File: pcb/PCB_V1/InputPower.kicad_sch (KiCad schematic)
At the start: 15 parts, among them J901 12 V IN / 25 A design, Q901 NTMFS5C628NLT1G, U901 LM74700QDBVRQ1

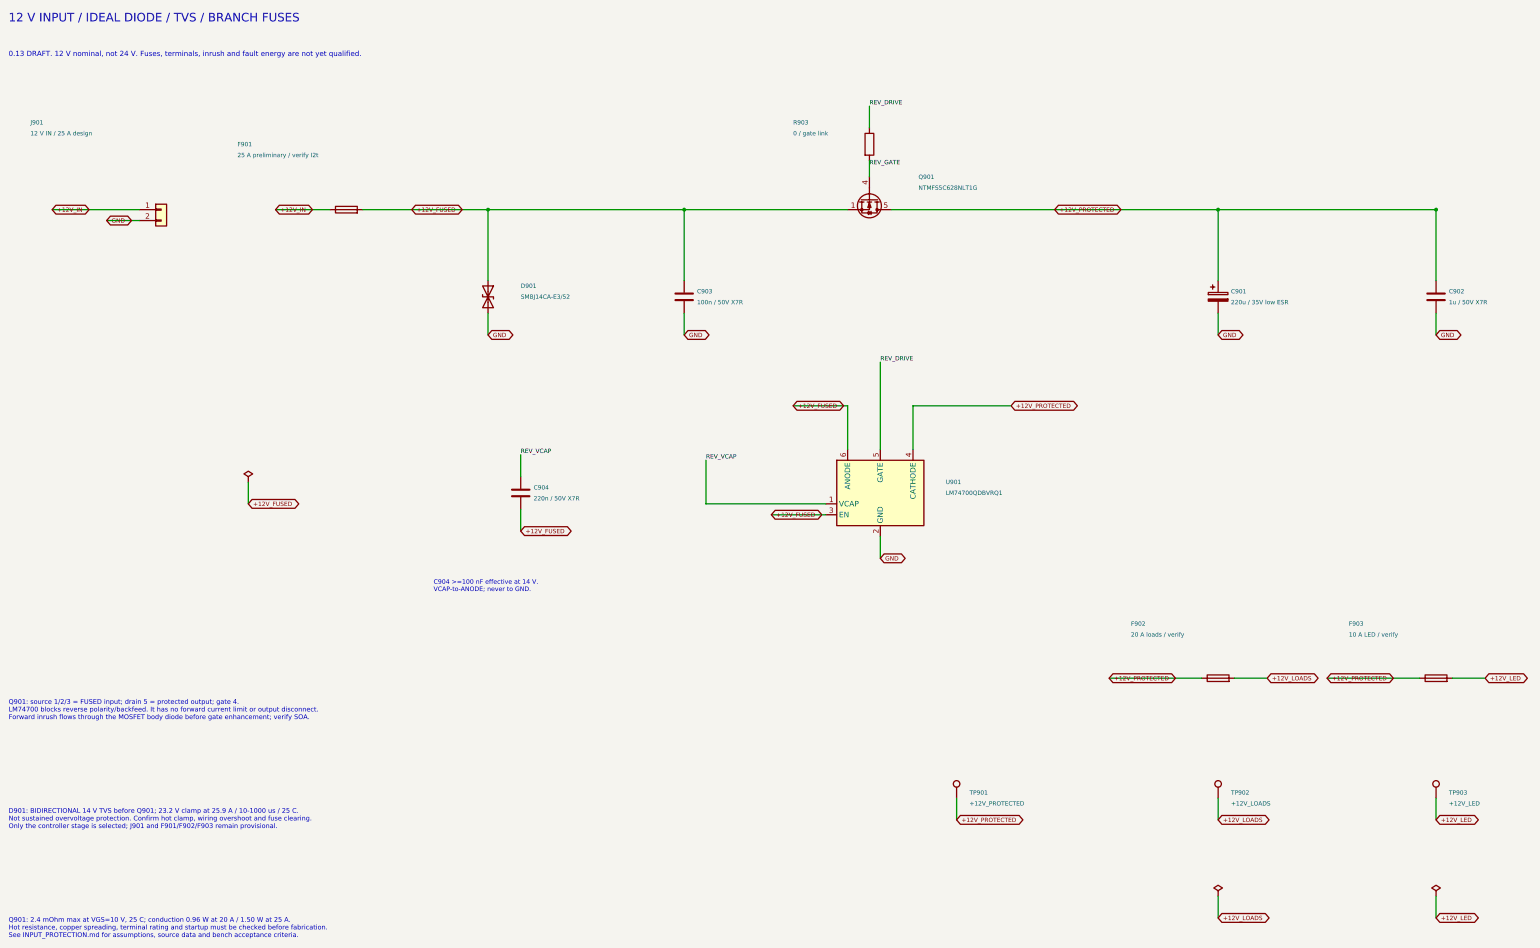
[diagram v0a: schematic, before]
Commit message: pcb: move board to 24 V input with 12 V aux buck and merged LED bar channel
Revision 0.14 of PCB_V1 (see pcb/PCB_V1/REDESIGN_24V.md):
- 24 V input on keyed XT60PW-M (pin 1 GND, pin 2 +24V); LM74700, input
  MOSFET and F901 removed; SMBJ26CA TVS; 220 uF/50 V bulk
- ATM mini-blade fuses in XF-508P-B-B holders: F902 10 A loads, F903 7.5 A LED
- new LMR16020 24 V -> 12 V aux buck (500 kHz) feeding PC fans, the
  UCC27524A heater gate driver and the TPS54202 3.3 V buck; TPS70950 removed
- heater and pump on 24 V: SMBJ30A drain TVS, AO3422 + SS36 pump stage
- LED CH1 panel keeps SRP1770TA/0.027 R/1k, switch now CSD19534Q5A;
  CH2 drives both identical bars in parallel (J721 || J731, 0.40 R);
  third AL8853 channel removed
- TS-1187A buttons, DORABO/KANGNEX terminals
- project library: LMR16020 and CSD19534Q5A symbols, TI DQJ and XF-508P
  footprints
- verify_netlist.py / verify_board.py / analyze_*.py updated for 24 V;
  new sync_board.py updates the unrouted staging board from the netlist
- ERC 0/0; netlist, board and sizing checks pass; DRC only the 12 known
  ESP32 drill sizes plus unrouted connections; 163 components

Co-Authored-By: Claude Opus 5.5 <noreply@anthropic.com>
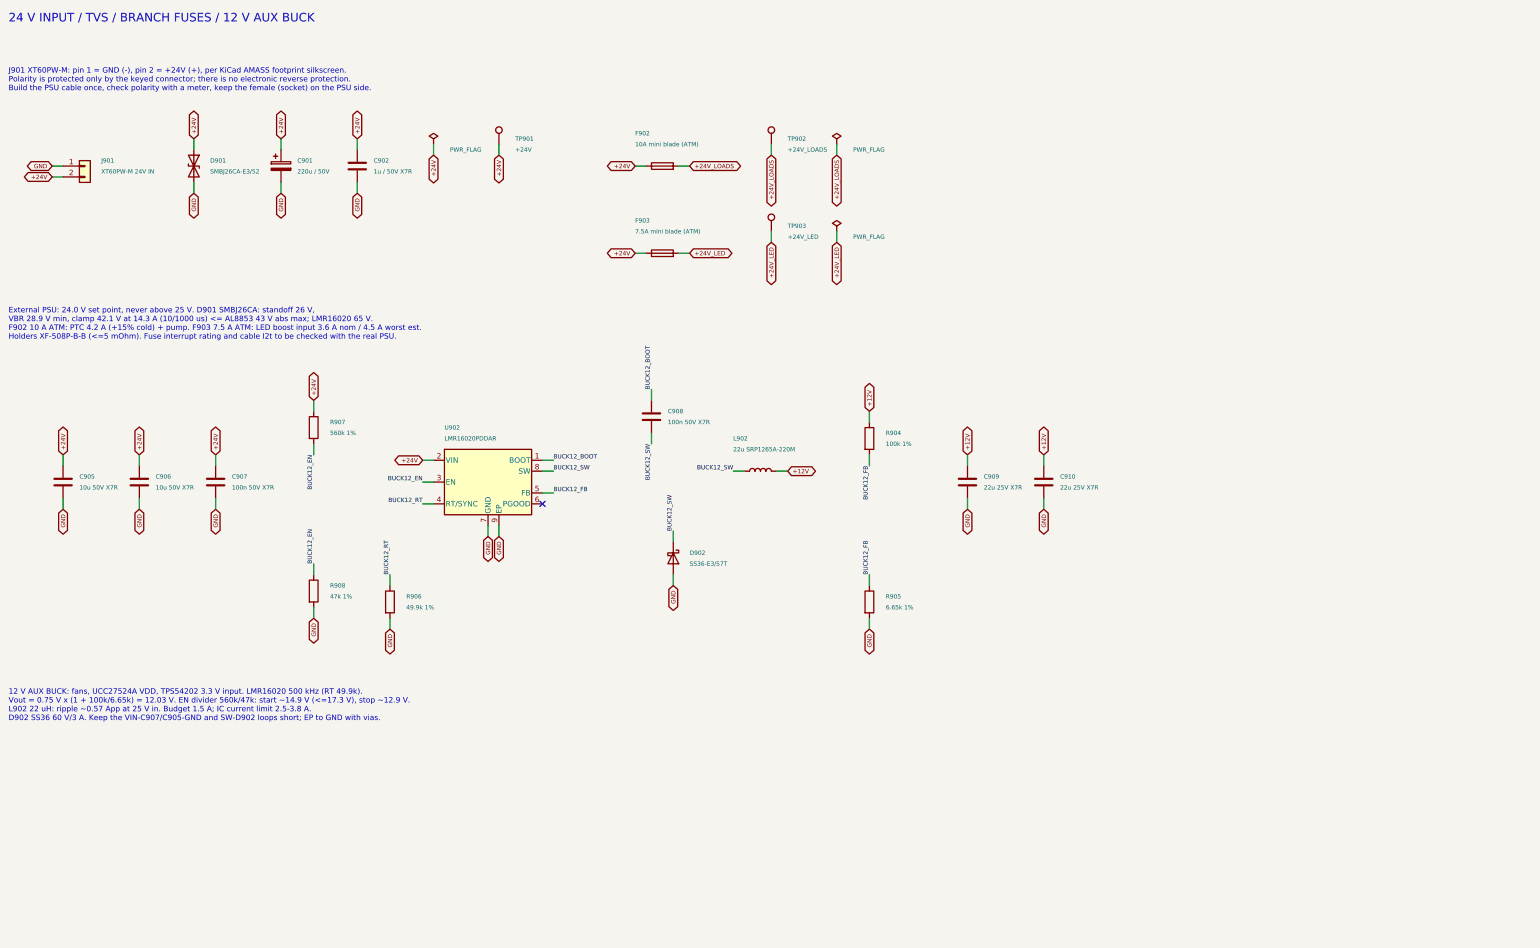
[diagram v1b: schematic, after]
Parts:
- removed C903: 100n / 50V X7R, Capacitor_SMD:C_0805_2012Metric, symbol Device:C
- removed C904: 220n / 50V X7R, Capacitor_SMD:C_0805_2012Metric, symbol Device:C
- removed F901: 25 A preliminary / verify I2t, Fuse:Fuse_2920_7451Metric, symbol Device:Fuse
- removed Q901: NTMFS5C628NLT1G, Package_SO:ONSemi_SO-8FL_488AA, symbol GrowBox:NTMFS5C628NL
- removed R903: 0 / gate link, Resistor_SMD:R_0603_1608Metric, symbol Device:R
- removed U901: LM74700QDBVRQ1, Package_TO_SOT_SMD:SOT-23-6, symbol Power_Management:LM74700
- added C905, C906: 10u 50V X7R, Capacitor_SMD:C_1210_3225Metric, symbol Device:C
- added C907, C908: 100n 50V X7R, Capacitor_SMD:C_0603_1608Metric, symbol Device:C
- added C909, C910: 22u 25V X7R, Capacitor_SMD:C_1210_3225Metric, symbol Device:C
- added D902: SS36-E3/57T, Diode_SMD:D_SMC, symbol Device:D_Schottky
- added L902: 22u SRP1265A-220M, GrowBox:L_Bourns_SRP1265A, symbol Device:L
- added R904: 100k 1%, Resistor_SMD:R_0603_1608Metric, symbol Device:R
- added R905: 6.65k 1%, Resistor_SMD:R_0603_1608Metric, symbol Device:R
- added R906: 49.9k 1%, Resistor_SMD:R_0603_1608Metric, symbol Device:R
- added R907: 560k 1%, Resistor_SMD:R_0603_1608Metric, symbol Device:R
- added R908: 47k 1%, Resistor_SMD:R_0603_1608Metric, symbol Device:R
- added U902: LMR16020PDDAR, Package_SO:SOIC-8-1EP_3.9x4.9mm_P1.27mm_EP2.95x4.9mm_Mask2.71x3.4mm, symbol GrowBox:LMR16020
- C901: value 220u / 35V low ESR -> 220u / 50V; LCSC (none) -> C178549; MPN (none) -> EEEFK1H221P; Manufacturer (none) -> Panasonic
- D901: value SMBJ14CA-E3/52 -> SMBJ26CA-E3/52; LCSC (none) -> C515606; MPN SMBJ14CA-E3/52 -> SMBJ26CA-E3/52
- F902: value 20 A loads / verify -> 10A mini blade (ATM); footprint Fuse:Fuse_2920_7451Metric -> GrowBox:Fuseholder_Blade_Mini_XFCN_XF-508P; LCSC (none) -> C19727305; MPN (none) -> XF-508P-B-B; Manufacturer (none) -> XFCN
- F903: value 10 A LED / verify -> 7.5A mini blade (ATM); footprint Fuse:Fuse_2920_7451Metric -> GrowBox:Fuseholder_Blade_Mini_XFCN_XF-508P; LCSC (none) -> C19727305; MPN (none) -> XF-508P-B-B; Manufacturer (none) -> XFCN
- J901: value 12 V IN / 25 A design -> XT60PW-M 24V IN; footprint TerminalBlock_Phoenix:TerminalBlock_Phoenix_MKDS-1,5-2-5.08_1x02_P5.08mm_Horizontal -> Connector_AMASS:AMASS_XT60PW-M_1x02_P7.20mm_Horizontal; LCSC (none) -> C98732; MPN (none) -> XT60PW-M; Manufacturer (none) -> Changzhou Amass
- TP901: value +12V_PROTECTED -> +24V
- TP902: value +12V_LOADS -> +24V_LOADS
- TP903: value +12V_LED -> +24V_LED
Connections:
- net +12V_IN is gone; now on net GND: J901.1 (Pin_1)
- net +12V_PROTECTED is gone; now on net +24V: C901.1, C902.1, F902.1, F903.1, TP901.1
- net GND: now also C905.2, C906.2, C907.2, C909.2, C910.2, D902.2 (A), R905.2, R906.2, R908.2, U902.7 (GND), U902.9 (EP); no longer J901.2 (Pin_2)
- net +12V_FUSED renamed +24V
- net +24V: now also J901.2 (Pin_2), C905.1, C906.1, C907.1, R907.1, U902.2 (VIN)
- net +12V_LED renamed +24V_LED
- net +12V_LOADS renamed +24V_LOADS
- new net +12V: C909.1, C910.1, L902.2, R904.1
- new net BUCK12_BOOT: C908.1, U902.1 (BOOT)
- new net BUCK12_EN: R907.2, R908.1, U902.3 (EN)
- new net BUCK12_FB: R904.2, R905.1, U902.5 (FB)
- new net BUCK12_RT: R906.1, U902.4 (RT/SYNC)
- new net BUCK12_SW: C908.2, D902.1 (K), L902.1, U902.8 (SW)
- no-connect marks 0 -> 1
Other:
- note added: "12 V AUX BUCK: fans, UCC27524A VDD, TPS54202 3.3 V input. LMR16020 500 kHz (RT 49.9k). Vout = 0.75 V x (1 + 100k/6.65k) = 12.03 V. EN divider 560k/47k: start ~14.9 V (<=17.3 V), stop ~12.9 V. L902 22 uH: ripple ~0.57 App at 25 V in. Budget 1.5 A; IC current limit 2.5-3.8 A. D902 SS36 60 V/3 A. Keep the VIN-C907/C905-GND and SW-D902 loops short; EP to GND with vias."
- note added: "24 V INPUT / TVS / BRANCH FUSES / 12 V AUX BUCK"
- note added: "External PSU: 24.0 V set point, never above 25 V. D901 SMBJ26CA: standoff 26 V, VBR 28.9 V min, clamp 42.1 V at 14.3 A (10/1000 us) <= AL8853 43 V abs max; LMR16020 65 V. F902 10 A ATM: PTC 4.2 A (+15% cold) + pump. F903 7.5 A ATM: LED boost input 3.6 A nom / 4.5 A worst est. Holders XF-508P-B-B (<=5 mOhm). Fuse interrupt rating and cable I2t to be checked with the real PSU."
- note added: "J901 XT60PW-M: pin 1 = GND (-), pin 2 = +24V (+), per KiCad AMASS footprint silkscreen. Polarity is protected only by the keyed connector; there is no electronic reverse protection. Build the PSU cable once, check polarity with a meter, keep the female (socket) on the PSU side."
- note removed: "0.13 DRAFT. 12 V nominal, not 24 V. Fuses, terminals, inrush and fault energy are not yet qualified."
- note removed: "12 V INPUT / IDEAL DIODE / TVS / BRANCH FUSES"
- note removed: "C904 >=100 nF effective at 14 V. VCAP-to-ANODE; never to GND."
- note removed: "D901: BIDIRECTIONAL 14 V TVS before Q901; 23.2 V clamp at 25.9 A / 10-1000 us / 25 C. Not sustained overvoltage protection. Confirm hot clamp, wiring overshoot and fuse clearing. Only the controller stage is selected; J901 and F901/F902/F903 remain provisional."
- note removed: "Q901: 2.4 mOhm max at VGS=10 V, 25 C; conduction 0.96 W at 20 A / 1.50 W at 25 A. Hot resistance, copper spreading, terminal rating and startup must be checked before fabrication. See INPUT_PROTECTION.md for assumptions, source data and bench acceptance criteria."
- note removed: "Q901: source 1/2/3 = FUSED input; drain 5 = protected output; gate 4. LM74700 blocks reverse polarity/backfeed. It has no forward current limit or output disconnect. Forward inrush flows through the MOSFET body diode before gate enhancement; verify SOA."
- title: 06 - 12 V input protection and branch fuses -> 06 - 24 V input, branch fuses, 12 V auxiliary buck
- moved on the sheet: C901, C902, D901, F902, F903, J901, TP901, TP902, TP903
